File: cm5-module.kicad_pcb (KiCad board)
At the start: 4 copper layers, 100 x 100 mm, 4 parts, among them J1 09031967921, U1 TPD2E2U06DCK

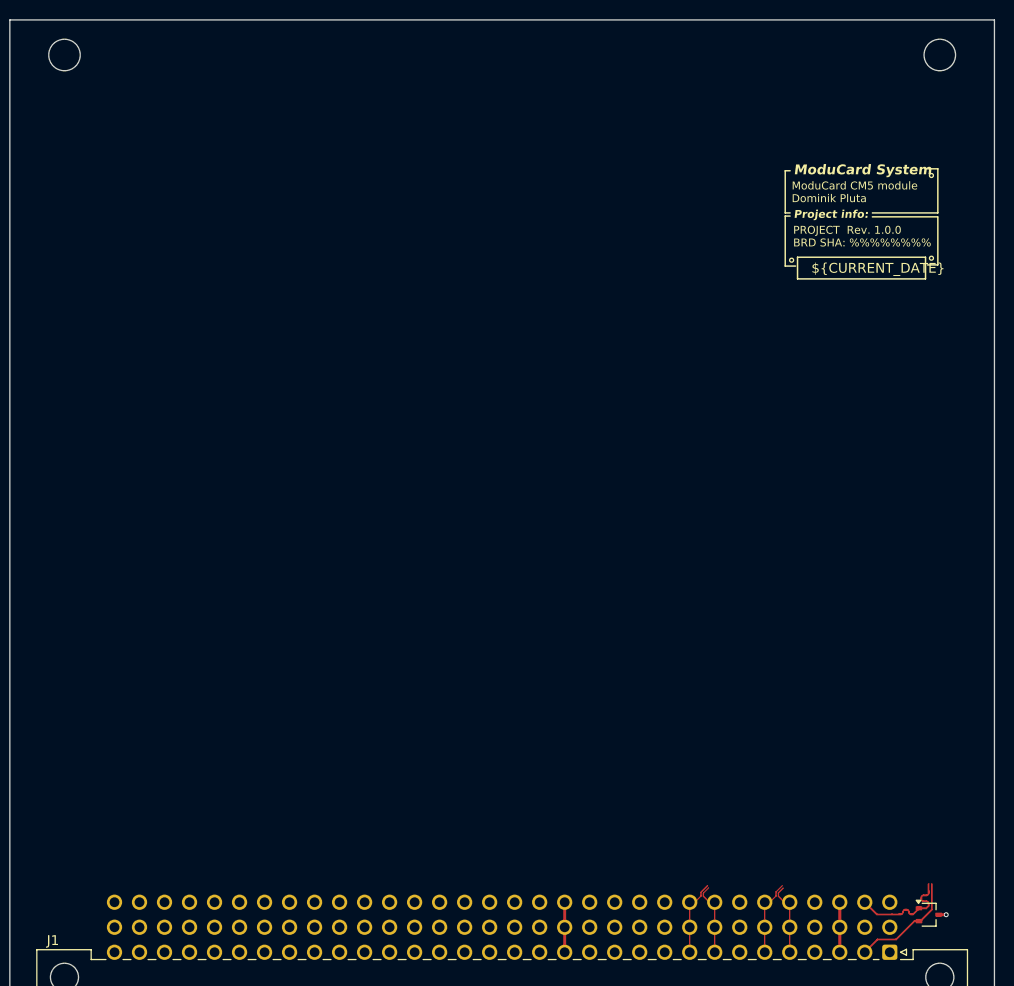
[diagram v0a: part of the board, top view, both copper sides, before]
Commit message: [#1] WIP: Change components to ones from the global library, refactor schematic
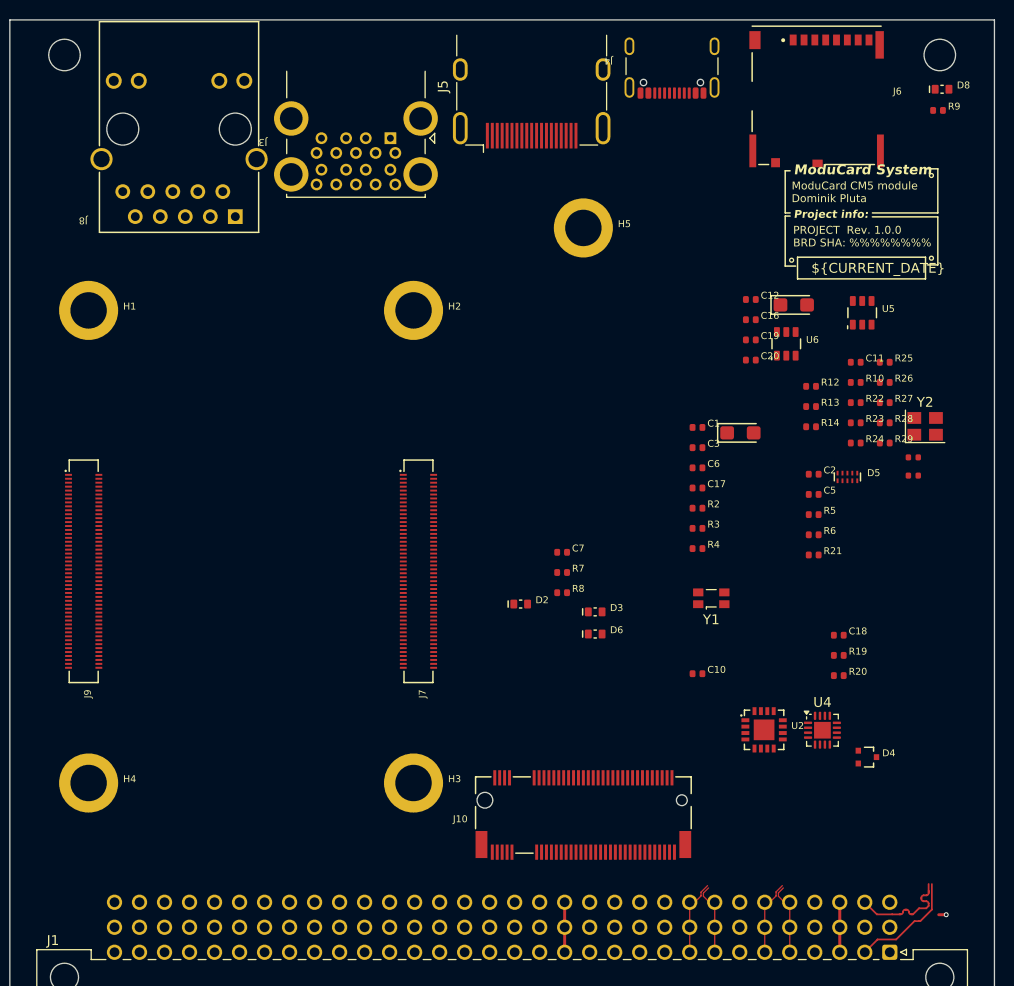
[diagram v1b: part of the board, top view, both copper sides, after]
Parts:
- removed U1: TPD2E2U06DCK, Package_TO_SOT_SMD:SOT-323_SC-70
- added A1: RPi CM5, DW-footprints:CM5, F.Cu at (80.4, 128.8)
- added C1: C-100n-0402, DW-footprints:C_0402_1005Metric, F.Cu at (109.2, 92.7)
- added C10: C-100n-0402, DW-footprints:C_0402_1005Metric, F.Cu at (109.2, 117.7)
- added C11: C-100n-0402, DW-footprints:C_0402_1005Metric, F.Cu at (125.3, 86.1)
- added C12: C-100n-0402, DW-footprints:C_0402_1005Metric, F.Cu at (114.6, 79.7)
- added C13: 10uF, PCM_JLCPCB:C_0402, F.Cu at (131.1, 95.7)
- added C14: 1uF, PCM_JLCPCB:C_0402, F.Cu at (131.1, 97.6)
- added C15: 10uF, PCM_JLCPCB:C_CASE-A-3216-18(mm), F.Cu at (119.0, 80.2)
- added C16: C-4u7-0402, DW-footprints:C_0402_1005Metric, F.Cu at (114.6, 81.7)
- added C17: C-4u7-0402, DW-footprints:C_0402_1005Metric, F.Cu at (109.2, 98.8)
- added C18: C-100n-0402, DW-footprints:C_0402_1005Metric, F.Cu at (123.6, 113.8)
- added C19: C-4u7-0402, DW-footprints:C_0402_1005Metric, F.Cu at (114.6, 83.8)
- added C2: C-100n-0402, DW-footprints:C_0402_1005Metric, F.Cu at (121.0, 97.4)
- added C20: C-100n-0402, DW-footprints:C_0402_1005Metric, F.Cu at (114.6, 85.8)
- added C3: C-100n-0402, DW-footprints:C_0402_1005Metric, F.Cu at (109.2, 94.7)
- added C4: 10uF, PCM_JLCPCB:C_CASE-A-3216-18(mm), F.Cu at (113.6, 93.2)
- added C5: C-100n-0402, DW-footprints:C_0402_1005Metric, F.Cu at (121.0, 99.5)
- added C6: C-4u7-0402, DW-footprints:C_0402_1005Metric, F.Cu at (109.2, 96.8)
- added C7: C-100n-0402, DW-footprints:C_0402_1005Metric, F.Cu at (95.5, 105.4)
- added D2: LED-R-0603_KT-0603R, DW-footprints:LED_0603_1608Metric_R, F.Cu at (91.3, 110.6)
- added D3: LED-R-0603_KT-0603R, DW-footprints:LED_0603_1608Metric_R, F.Cu at (98.8, 111.4)
- added D4: TPD2E2U06DCKR, DW-footprints:SOT-323, F.Cu at (126.5, 126.2)
- added D5: PUSB3F96X, DW-footprints:SOT1176-1, F.Cu at (124.4, 97.7)
- added D6: LED-R-0603_KT-0603R, DW-footprints:LED_0603_1608Metric_R, F.Cu at (98.8, 113.7)
- added D8: LED-R-0603_KT-0603R, DW-footprints:LED_0603_1608Metric_R, F.Cu at (134.1, 58.3)
- added H1: Spacer_M2.5_H3mm_9774030151R, DW-footprints:Spacer_M2.5_H3mm_9774030151R, F.Cu at (47.4, 80.8)
- added H2: Spacer_M2.5_H3mm_9774030151R, DW-footprints:Spacer_M2.5_H3mm_9774030151R, F.Cu at (80.4, 80.8)
- added H3: Spacer_M2.5_H3mm_9774030151R, DW-footprints:Spacer_M2.5_H3mm_9774030151R, F.Cu at (80.4, 128.8)
- added H4: Spacer_M2.5_H3mm_9774030151R, DW-footprints:Spacer_M2.5_H3mm_9774030151R, F.Cu at (47.4, 128.8)
- added H5: Spacer_M2.5_H2.5mm_9774025151R, DW-footprints:Spacer_M2.5_H2.5mm_9774025151R, F.Cu at (97.6, 72.4)
- added J10: Bus_M.2_1-2199230-6, DW-footprints:Bus_M.2_Socket_Key_M_TE_1-2199230-6, F.Cu at (97.6, 132.0)
- added J3: USB-A_USB-303WSD-BRY, DW-footprints:2xUSB3.0_USB-303WSD-BRY, F.Cu at (78.0, 63.3)
- added J4: USB-C_USB-310F-B-SU, DW-footprints:USB-C-receptacle-16P_USB-310F-B-SU, F.Cu at (106.6, 55.0)
- added J5: HDMI_A, Connector_Video:HDMI_A_Molex_208658-1001_Horizontal, F.Cu at (92.4, 59.8)
- added J6: MicroSD_5033981892, DW-footprints:MicroSD_5033981892, F.Cu at (121.3, 58.9)
- added J7: CM5_101-200_3mm-stack, DW-footprints:Conn_Socket_Hirose_DF40_2x50_DF40HC-3.0-100DS-0.4V, F.Cu at (80.9, 107.3)
- added J8: RJ45_HC612601A-M893-A, DW-footprints:RJ45_HC612601A-M893-A, F.Cu at (62.3, 71.3)
- added J9: CM5_1-100_3mm-stack, DW-footprints:Conn_Socket_Hirose_DF40_2x50_DF40HC-3.0-100DS-0.4V, F.Cu at (46.9, 107.3)
- added R10: R-1k-0402, DW-footprints:R_0402_1005Metric, F.Cu at (125.3, 88.1)
- added R12: R-10k-0402, DW-footprints:R_0402_1005Metric, F.Cu at (120.7, 88.5)
- added R13: R-10k-0402, DW-footprints:R_0402_1005Metric, F.Cu at (120.7, 90.6)
- added R14: R-10k-0402, DW-footprints:R_0402_1005Metric, F.Cu at (120.7, 92.6)
- added R19: R-1k-0402, DW-footprints:R_0402_1005Metric, F.Cu at (123.6, 115.8)
- added R2: R-0R-0402, DW-footprints:R_0402_1005Metric, F.Cu at (109.2, 100.9)
- added R20: R-1k-0402, DW-footprints:R_0402_1005Metric, F.Cu at (123.6, 117.9)
- added R21: R-5k1-0402, DW-footprints:R_0402_1005Metric, F.Cu at (121.0, 105.6)
- added R22: R-220r-0402, DW-footprints:R_0402_1005Metric, F.Cu at (125.3, 90.2)
- added R23: R-220r-0402, DW-footprints:R_0402_1005Metric, F.Cu at (125.3, 92.2)
- added R24: R-220r-0402, DW-footprints:R_0402_1005Metric, F.Cu at (125.3, 94.3)
- added R25: R-220r-0402, DW-footprints:R_0402_1005Metric, F.Cu at (128.2, 86.1)
- added R26: R-220r-0402, DW-footprints:R_0402_1005Metric, F.Cu at (128.2, 88.1)
- added R27: R-220r-0402, DW-footprints:R_0402_1005Metric, F.Cu at (128.2, 90.2)
- added R28: R-220r-0402, DW-footprints:R_0402_1005Metric, F.Cu at (128.2, 92.2)
- added R29: R-220r-0402, DW-footprints:R_0402_1005Metric, F.Cu at (128.2, 94.3)
- added R3: R-10k-0402, DW-footprints:R_0402_1005Metric, F.Cu at (109.2, 102.9)
- added R4: R-2k2-0402, DW-footprints:R_0402_1005Metric, F.Cu at (109.2, 105.0)
- added R5: R-330r-0402, DW-footprints:R_0402_1005Metric, F.Cu at (121.0, 101.5)
- added R6: R-5k1-0402, DW-footprints:R_0402_1005Metric, F.Cu at (121.0, 103.6)
- added R7: R-1k-0402, DW-footprints:R_0402_1005Metric, F.Cu at (95.5, 107.4)
- added R8: R-1k-0402, DW-footprints:R_0402_1005Metric, F.Cu at (95.5, 109.5)
- added R9: R-1k-0402, DW-footprints:R_0402_1005Metric, F.Cu at (133.6, 60.5)
- added U2: FT230XQ-R, DW-footprints:QFN-16-1EP_4x4mm_P0.65mm_EP2.15x2.15mm, F.Cu at (116.0, 123.4)
- added U4: CH334P, Package_DFN_QFN:QFN-16-1EP_3x3mm_P0.5mm_EP1.7x1.7mm, F.Cu at (121.9, 123.4)
- added U5: AP22615AWU-7, DW-footprints:TSOT-23-6, F.Cu at (125.9, 81.0)
- added U6: AP22615AWU-7, DW-footprints:TSOT-23-6, F.Cu at (118.2, 84.2)
- added Y1: SG-3030CM, Oscillator:Oscillator_SMD_SeikoEpson_SG3030CM, F.Cu at (110.6, 110.0)
- added Y2: 12Mhz, Crystal:Crystal_SMD_3225-4Pin_3.2x2.5mm, F.Cu at (132.3, 92.6)
- J1: value 09031967921 -> DIN-41612-connector_09031967921
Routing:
- net GND: track 0.76 -> 0.00 mm, vias 1 -> 0
- net /CM5/ETH.D4+: track 0.00 -> 0.76 mm, vias 0 -> 1

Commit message: [#1] Change components to ones from the global library, add debug console, refactor schematic
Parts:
- removed C13: 10uF, PCM_JLCPCB:C_0402
- removed C14: 1uF, PCM_JLCPCB:C_0402
- removed D2: LED-R-0603_KT-0603R, DW-footprints:LED_0603_1608Metric_R
- removed R10: R-1k-0402, DW-footprints:R_0402_1005Metric
- removed U4: CH334P, Package_DFN_QFN:QFN-16-1EP_3x3mm_P0.5mm_EP1.7x1.7mm
- added C23: C-100n-0402, DW-footprints:C_0402_1005Metric, F.Cu at (234.7, 111.6)
- added C8: C-4u7-0402, DW-footprints:C_0402_1005Metric, F.Cu at (234.7, 107.5)
- added C9: C-4u7-0402, DW-footprints:C_0402_1005Metric, F.Cu at (234.7, 109.6)
- added D7: LED-R-0603_KT-0603R, DW-footprints:LED_0603_1608Metric_R, F.Cu at (238.0, 112.5)
- added R11: R-1k-0402, DW-footprints:R_0402_1005Metric, F.Cu at (234.7, 113.7)
- added U1: CH334P, DW-footprints:QFN-16-1EP_3x3mm_P0.5mm_EP1.75x1.75mm, F.Cu at (238.6, 109.0)
- J1: footprint Connector_DIN:DIN41612_R_3x32_Female_Horizontal_THT -> DW-footprints:Conn_DIN_41612_09031967921
- J3: footprint DW-footprints:2xUSB3.0_USB-303WSD-BRY -> DW-footprints:USB-A_Receptacle_USB-303WSD-BRY
- J4: footprint DW-footprints:USB-C-receptacle-16P_USB-310F-B-SU -> DW-footprints:USB-C-Receptacle_USB-310F-B-SU
- Y1: value SG-3030CM -> Oscillator_32.768kHz_OK2EL89CJI-111YLC-32.768K; footprint Oscillator:Oscillator_SMD_SeikoEpson_SG3030CM -> DW-footprints:Crystal_SMD_3225-4Pin_3.2x2.5mm
- Y2: value 12Mhz -> X322512MSB4SI; footprint Crystal:Crystal_SMD_3225-4Pin_3.2x2.5mm -> DW-footprints:Crystal_SMD_3225-4Pin_3.2x2.5mm
- moved Y2 144.8 mm to (272.5, 128.7)
- moved C1 142.3 mm to (249.5, 116.2)
- moved C12 142.3 mm to (254.9, 103.2)
- moved C15 142.3 mm to (259.3, 103.8)
- moved C16 142.3 mm to (254.9, 105.3)
- moved C17 142.3 mm to (249.5, 122.4)
- moved C19 142.3 mm to (254.9, 107.3)
- moved C2 142.3 mm to (261.3, 121.0)
- moved C20 142.3 mm to (254.9, 109.4)
- moved C3 142.3 mm to (249.5, 118.3)
- moved C4 142.3 mm to (253.9, 116.8)
- moved C5 142.3 mm to (261.3, 123.0)
- moved C6 142.3 mm to (249.5, 120.3)
- moved D5 142.3 mm to (264.7, 121.2)
- moved R12 142.3 mm to (261.0, 112.0)
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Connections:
- net /Backplane/CAN1.+ renamed /Backplane/CAN_1.+
- net /Backplane/CAN1.- renamed /Backplane/CAN_1.-
- net /Backplane/CAN2.+ renamed /Backplane/CAN_2.+
- net /Backplane/CAN2.- renamed /Backplane/CAN_2.-
- net /CM5/HDMI0.CEC renamed /CM5/HDMI_0.CEC
- net /CM5/HDMI0.CLK+ renamed /CM5/HDMI_0.CLK+
- net /CM5/HDMI0.CLK- renamed /CM5/HDMI_0.CLK-
- net /CM5/HDMI0.D0+ renamed /CM5/HDMI_0.D0+
- net /CM5/HDMI0.D0- renamed /CM5/HDMI_0.D0-
- net /CM5/HDMI0.D1+ renamed /CM5/HDMI_0.D1+
- net /CM5/HDMI0.D1- renamed /CM5/HDMI_0.D1-
- net /CM5/HDMI0.D2+ renamed /CM5/HDMI_0.D2+
- net /CM5/HDMI0.D2- renamed /CM5/HDMI_0.D2-
- net /CM5/HDMI0.HOTPLUG renamed /CM5/HDMI_0.HOTPLUG
- net /CM5/HDMI0.SCL renamed /CM5/HDMI_0.SCL
- net /CM5/HDMI0.SDA renamed /CM5/HDMI_0.SDA
- net /CM5/HDMI1.CEC renamed /CM5/HDMI_1.CEC
- net /CM5/HDMI1.CLK+ renamed /CM5/HDMI_1.CLK+
- net /CM5/HDMI1.CLK- renamed /CM5/HDMI_1.CLK-
- net /CM5/HDMI1.D0+ renamed /CM5/HDMI_1.D0+
- net /CM5/HDMI1.D0- renamed /CM5/HDMI_1.D0-
- net /CM5/HDMI1.D1+ renamed /CM5/HDMI_1.D1+
- net /CM5/HDMI1.D1- renamed /CM5/HDMI_1.D1-
- net /CM5/HDMI1.D2+ renamed /CM5/HDMI_1.D2+
- net /CM5/HDMI1.D2- renamed /CM5/HDMI_1.D2-
- net /CM5/HDMI1.HOTPLUG renamed /CM5/HDMI_1.HOTPLUG
- net /CM5/HDMI1.SCL renamed /CM5/HDMI_1.SCL
- net /CM5/HDMI1.SDA renamed /CM5/HDMI_1.SDA
- net /CM5/MIPI0.CLK+ renamed /CM5/MIPI_0.CLK+
- net /CM5/MIPI0.CLK- renamed /CM5/MIPI_0.CLK-
- net /CM5/MIPI0.D0+ renamed /CM5/MIPI_0.D0+
- net /CM5/MIPI0.D0- renamed /CM5/MIPI_0.D0-
- net /CM5/MIPI0.D1+ renamed /CM5/MIPI_0.D1+
- net /CM5/MIPI0.D1- renamed /CM5/MIPI_0.D1-
- net /CM5/MIPI0.D2+ renamed /CM5/MIPI_0.D2+
- net /CM5/MIPI0.D2- renamed /CM5/MIPI_0.D2-
- net /CM5/MIPI0.D3+ renamed /CM5/MIPI_0.D3+
- net /CM5/MIPI0.D3- renamed /CM5/MIPI_0.D3-
- net /CM5/MIPI1.CLK+ renamed /CM5/MIPI_1.CLK+
- net /CM5/MIPI1.CLK- renamed /CM5/MIPI_1.CLK-
- net /CM5/MIPI1.D0+ renamed /CM5/MIPI_1.D0+
- net /CM5/MIPI1.D0- renamed /CM5/MIPI_1.D0-
- net /CM5/MIPI1.D1+ renamed /CM5/MIPI_1.D1+
- net /CM5/MIPI1.D1- renamed /CM5/MIPI_1.D1-
- net /CM5/MIPI1.D2+ renamed /CM5/MIPI_1.D2+
- net /CM5/MIPI1.D2- renamed /CM5/MIPI_1.D2-
- net /CM5/MIPI1.D3+ renamed /CM5/MIPI_1.D3+
- net /CM5/MIPI1.D3- renamed /CM5/MIPI_1.D3-
- net /USB hub/USBOUT1.D+ renamed /USB hub/USB_1.D-
- net /USB hub/USBOUT1.D- renamed /USB hub/USB_1.D+
- net /USB hub/USBOUT2.D+ renamed /USB hub/USB_2.D-
- net /USB hub/USBOUT2.D- renamed /USB hub/USB_2.D+
- net /USB hub/USBOUT3.D+ renamed /USB hub/USB_3.D-
- net /USB hub/USBOUT3.D- renamed /USB hub/USB_3.D+
- net Net-(J10-LED) renamed /M.2/LED
- C11 pad 2: Net-(U4-3V3) -> +3V3_M2
- D8 pad 2: unconnected-(D8-A-Pad2) -> +3V3_M2
- H5 pad 1: unconnected-(H5-Pad1) -> GND
- J10 pad 12: Net-(J10-3V3-Pad12) -> +3V3_M2
- J10 pad 14: Net-(J10-3V3-Pad12) -> +3V3_M2
- J10 pad 16: Net-(J10-3V3-Pad12) -> +3V3_M2
- J10 pad 18: Net-(J10-3V3-Pad12) -> +3V3_M2
- J10 pad 2: Net-(J10-3V3-Pad12) -> +3V3_M2
- J10 pad 4: Net-(J10-3V3-Pad12) -> +3V3_M2
- J10 pad 68: unconnected-(J10-SUSCLK-Pad68) -> /M.2/SUSCLK
- J10 pad 70: Net-(J10-3V3-Pad12) -> +3V3_M2
- J10 pad 72: Net-(J10-3V3-Pad12) -> +3V3_M2
- J10 pad 74: Net-(J10-3V3-Pad12) -> +3V3_M2
- R22 pad 2: /USB hub/USBOUT1_R.D- -> /USB hub/USB_1_R.D+
- R23 pad 2: /USB hub/USBOUT1_R.D+ -> /USB hub/USB_1_R.D-
- R24 pad 2: /USB hub/USBOUT2_R.D- -> /USB hub/USB_2_R.D+
- R25 pad 2: /USB hub/USBOUT2_R.D+ -> /USB hub/USB_2_R.D-
- R26 pad 2: /USB hub/USBOUT3_R.D- -> /USB hub/USB_3_R.D+
- R27 pad 2: /USB hub/USBOUT3_R.D+ -> /USB hub/USB_3_R.D-
- R28 pad 1: /USB hub/USBOUT4.D- -> /Backplane/BACKPLANE.D+
- R28 pad 2: /USB hub/USBOUT4_R.D- -> /USB hub/USB_4_R.D+
- R29 pad 1: /USB hub/USBOUT4.D+ -> /Backplane/BACKPLANE.D-
- R29 pad 2: /USB hub/USBOUT4_R.D+ -> /USB hub/USB_4_R.D-
- Y1 pad 1: unconnected-(Y1-VIO-Pad1) -> +3V3_M2
- Y1 pad 3: unconnected-(Y1-OUT-Pad3) -> /M.2/SUSCLK
- Y1 pad 4: unconnected-(Y1-Vcc-Pad4) -> +3V3_M2
- Y2 pad 1: Net-(U4-XO) -> /USB hub/XO
- Y2 pad 3: Net-(U4-XI) -> /USB hub/XI
